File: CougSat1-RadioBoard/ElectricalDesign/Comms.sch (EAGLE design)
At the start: 416 parts, among them J1 230mm Antenna, J2 CougSat Card, J3 700mm Antenna, J4 SWD, Q1 CSD25402Q3A, Q12 DMN53D0LDW, Q2 CSD25402Q3A, Q3 DMN53D0LDW, Q9 DMN53D0LDW, U1 INA199C1, U10 HMC452QS16G, U11 AD8515, U12 AD7291, U13 AD8515, U14 LP5907MFX-3.1, U15 AD9761, U16 TXS0102DQM, U18 TXS0102DQM, U19 MMZ09332B, U2 LP5907MFX-3.1, U20 ADF4360, U21 HMC545A, U22 AD9761, U23 MAAM-011229, U24 AD8515, U25 MAAM-011229, U26 AD8345, U28 AD8348, U29 AD7291, U3 TPS61236, U30 TXS0102DQM, U31 MAAM-011229, U32 AD8515, U35 TXS0102DQM, U36 ADF4360, U37 MAAM-011229, U39 AD8515, U4 AD8346, U40 AD8515, U42 TXS0102DQM, U43 INA199C2, U44 TXS0102DQM, U45 TXS0102DQM, U46 TXS0102DQM, U47 TXS0102DQM, U48 AD7291, U49 AD8515, U5 ADF4360, U50 INA199C2, U51 LP5907MFX-3.1, U52 INA199C2, U53 INA199C1, U54 TXS0102DQM, U55 TXS0102DQM, U6 STM32L496VGT, U7 GRF2133, U8 IS25LP016D, U9 IS25LP016D, Y1 19.68MHz ±2.5ppm, Y2 8MHz ±10ppm, Y3 32.768kHz ±10ppm, Y4 19.68MHz ±2.5ppm, Y5 19.68MHz ±2.5ppm

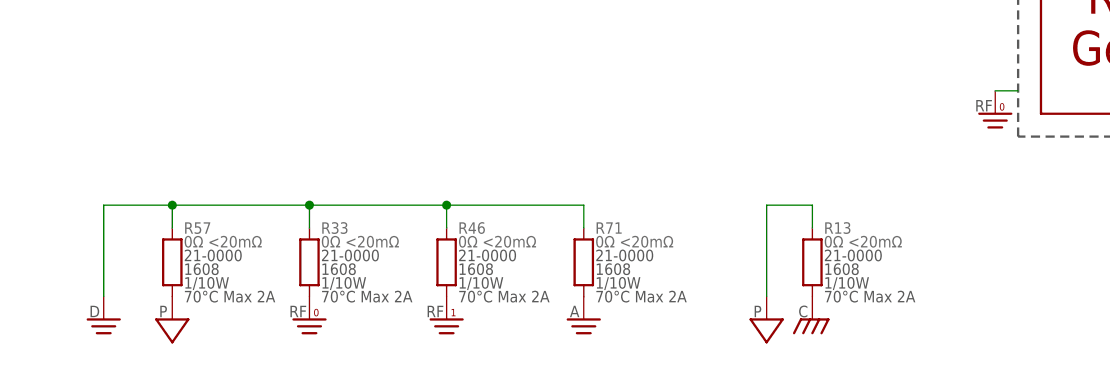
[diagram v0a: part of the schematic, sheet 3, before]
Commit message: Updated layout constraints and tests
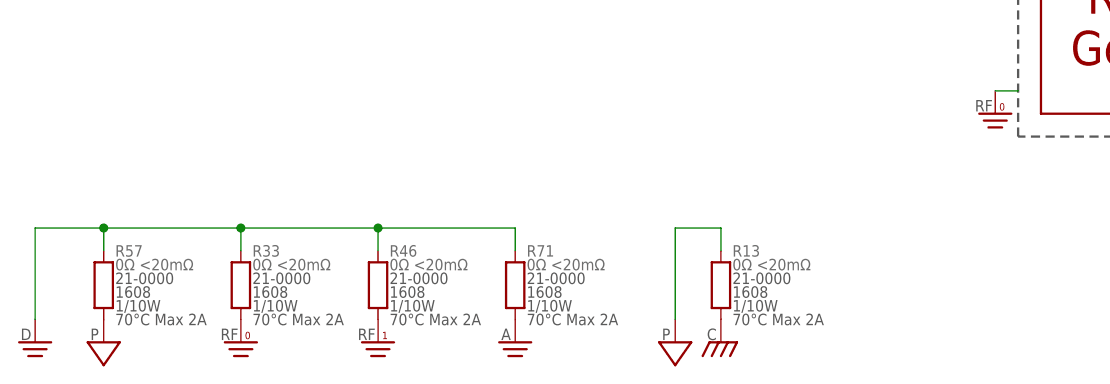
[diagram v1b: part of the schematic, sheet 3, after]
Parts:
- added RN4: 5kΩ 0.1%, CougsInSpace-Resistors:RES-H-PAIRED-5K-1616
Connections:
- net PA_PDET-700: now also RN4.B1
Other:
- moved on the sheet: C100, C93, FB6, R13, R33, R46, R57, R71, TP2

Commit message: Began part placement
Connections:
- removed net 3.3V_2: U20.AVDD, U20.CE, U20.DVDD, U20.VVCO
- net 3.1V_2: now also U20.AVDD, U20.CE, U20.DVDD, U20.VVCO
- net 3.3V_0: now also J2POWER.PR_3.3V-0; no longer J2POWER.PWR_CTRL_SW
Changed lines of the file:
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@@
 <class number="0" name="default" width="0" drill="0">
 </class>
-<class number="1" name="50Ohm" width="0.3" drill="0">
-<clearance class="1" value="0.16"/>
+<class number="1" name="50Ohm" width="0.22" drill="0">
+<clearance class="1" value="0.5"/>
 </class>
-<class number="2" name="200Ohm" width="0.16" drill="0">
-<clearance class="2" value="0.3"/>
+<class number="2" name="200Ohm" width="0.25" drill="0">
+<clearance class="2" value="0.6"/>
 </class>
 <class number="3" name="Supplies" width="0.25" drill="0">
@@
 <part name="DIA32" library="CougsInSpace-Aesthetics" deviceset="DIAGRAM-CONNECT_DOT" device=""/>
 <part name="DIA41" library="CougsInSpace-Aesthetics" deviceset="DIAGRAM-CONNECT_DOT" device=""/>
-<part name="SUPPLY129" library="CougsInSpace-PowerSymbols" deviceset="3.3V-2" device=""/>
 <part name="C5" library="CougsInSpace-Capacitors" deviceset="CAP-POL-V" device="-4028" technology="-47UF" value="47µF"/>
 <part name="J1" library="CougsInSpace-Connectors" deviceset="COAX" device="-U.FL" value="230mm Antenna"/>
@@
 <part name="R13" library="CougsInSpace-Resistors" deviceset="RES-V" device="-1608" technology="-0" value="0Ω &lt;20mΩ"/>
 <part name="RN4" library="CougsInSpace-Resistors" deviceset="RES-H-PAIRED" device="-1616" technology="-5K" value="5kΩ 0.1%"/>
+<part name="SUPPLY129" library="CougsInSpace-PowerSymbols" deviceset="3.1V-2" device=""/>
 </parts>
 <sheets>
@@
 </segment>
 <segment>
-<pinref part="J2" gate="POWER" pin="PWR_CTRL_SW"/>
 <pinref part="SUPPLY86" gate="G$1" pin="3.3V_0"/>
-<wire x1="241.3" y1="182.88" x2="246.38" y2="182.88" width="0.1524" layer="91"/>
 <wire x1="246.38" y1="182.88" x2="246.38" y2="185.42" width="0.1524" layer="91"/>
+<pinref part="J2" gate="POWER" pin="PR_3.3V-0"/>
+<wire x1="241.3" y1="180.34" x2="246.38" y2="180.34" width="0.1524" layer="91"/>
+<wire x1="246.38" y1="180.34" x2="246.38" y2="182.88" width="0.1524" layer="91"/>
 </segment>
 </net>
@@
 <attribute name="SKU" x="229.87" y="144.272" size="1.27" layer="97" align="center-left"/>
 </instance>
-<instance part="SUPPLY129" gate="G$1" x="127" y="175.26" smashed="yes">
-<attribute name="VALUE" x="127" y="178.816" size="1.27" layer="96" align="center"/>
-</instance>
 <instance part="Y4" gate="G$1" x="101.6" y="170.18" smashed="yes">
 <attribute name="NAME" x="101.6" y="176.53" size="1.778" layer="95" align="center"/>
@@
 <instance part="SUPPLY181" gate="G$1" x="15.24" y="45.72" smashed="yes"/>
 <instance part="SUPPLY182" gate="G$1" x="15.24" y="7.62" smashed="yes"/>
+<instance part="SUPPLY129" gate="G$1" x="127" y="175.26" smashed="yes">
+<attribute name="VALUE" x="127" y="178.816" size="1.27" layer="96" align="center"/>
+</instance>
 </instances>
 <busses>
@@
 </segment>
 </net>
-<net name="3.3V_2" class="0">
-<segment>
-<pinref part="U20" gate="G$1" pin="AVDD"/>
-<wire x1="129.54" y1="172.72" x2="127" y2="172.72" width="0.1524" layer="91"/>
-<pinref part="U20" gate="G$1" pin="DVDD"/>
-<wire x1="129.54" y1="170.18" x2="127" y2="170.18" width="0.1524" layer="91"/>
-<wire x1="127" y1="170.18" x2="127" y2="172.72" width="0.1524" layer="91"/>
-<pinref part="U20" gate="G$1" pin="VVCO"/>
-<wire x1="129.54" y1="167.64" x2="127" y2="167.64" width="0.1524" layer="91"/>
-<wire x1="127" y1="167.64" x2="127" y2="170.18" width="0.1524" layer="91"/>
-<junction x="127" y="170.18"/>
-<wire x1="127" y1="172.72" x2="127" y2="175.26" width="0.1524" layer="91"/>
-<junction x="127" y="172.72"/>
-<pinref part="U20" gate="G$1" pin="CE"/>
-<wire x1="129.54" y1="149.86" x2="127" y2="149.86" width="0.1524" layer="91"/>
-<wire x1="127" y1="149.86" x2="127" y2="167.64" width="0.1524" layer="91"/>
-<junction x="127" y="167.64"/>
-<pinref part="SUPPLY129" gate="G$1" pin="3.3V_2"/>
-</segment>
-</net>
 <net name="RFCLK_REFIN-DEMOD" class="0">
 <segment>
@@
 <pinref part="SUPPLY441" gate="G$1" pin="3.1V_2"/>
 </segment>
+<segment>
+<pinref part="U20" gate="G$1" pin="AVDD"/>
+<wire x1="129.54" y1="172.72" x2="127" y2="172.72" width="0.1524" layer="91"/>
+<pinref part="U20" gate="G$1" pin="DVDD"/>
+<wire x1="129.54" y1="170.18" x2="127" y2="170.18" width="0.1524" layer="91"/>
+<wire x1="127" y1="170.18" x2="127" y2="172.72" width="0.1524" layer="91"/>
+<pinref part="U20" gate="G$1" pin="VVCO"/>
+<wire x1="129.54" y1="167.64" x2="127" y2="167.64" width="0.1524" layer="91"/>
+<wire x1="127" y1="167.64" x2="127" y2="170.18" width="0.1524" layer="91"/>
+<junction x="127" y="170.18"/>
+<wire x1="127" y1="172.72" x2="127" y2="175.26" width="0.1524" layer="91"/>
+<junction x="127" y="172.72"/>
+<pinref part="U20" gate="G$1" pin="CE"/>
+<wire x1="129.54" y1="149.86" x2="127" y2="149.86" width="0.1524" layer="91"/>
+<wire x1="127" y1="149.86" x2="127" y2="167.64" width="0.1524" layer="91"/>
+<junction x="127" y="167.64"/>
+<pinref part="SUPPLY129" gate="G$1" pin="3.1V_2"/>
+</segment>
 </net>

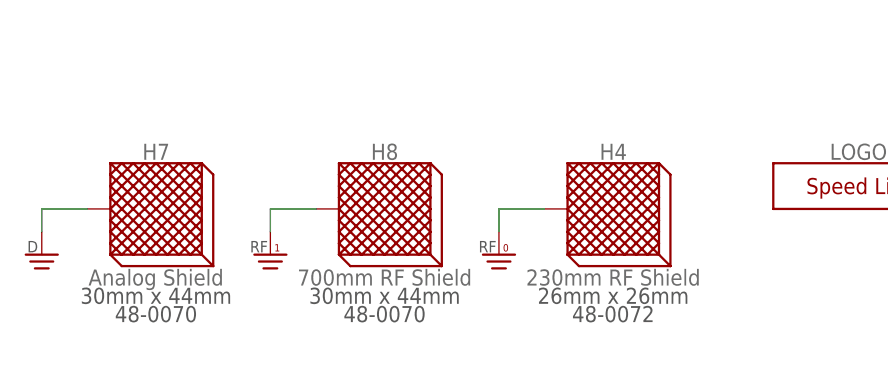
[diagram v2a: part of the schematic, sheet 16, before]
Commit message: Placed Comms parts
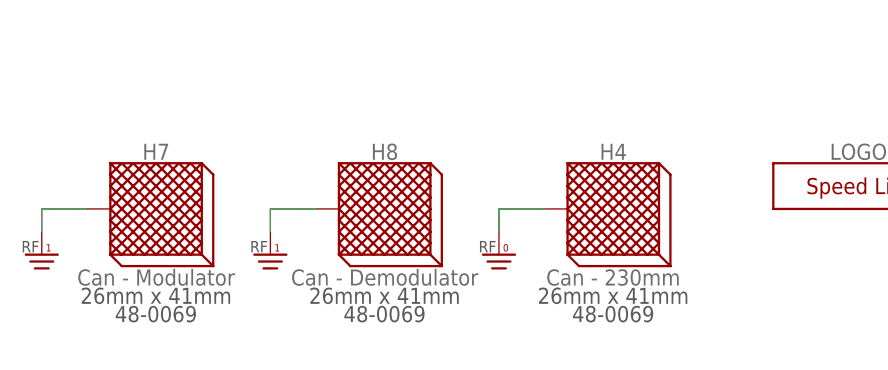
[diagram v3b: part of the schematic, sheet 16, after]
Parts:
- H4: value 230mm RF Shield -> Can - 230mm; device CougsInSpace-Hardware:SHIELDING-2626 -> CougsInSpace-Hardware:SHIELDING-2641
- H7: value Analog Shield -> Can - Modulator; device CougsInSpace-Hardware:SHIELDING-3044 -> CougsInSpace-Hardware:SHIELDING-2641
- H8: value 700mm RF Shield -> Can - Demodulator; device CougsInSpace-Hardware:SHIELDING-3044 -> CougsInSpace-Hardware:SHIELDING-2641
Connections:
- net DGND: no longer H7.SHIELD
- net RFGND-1: now also H7.SHIELD

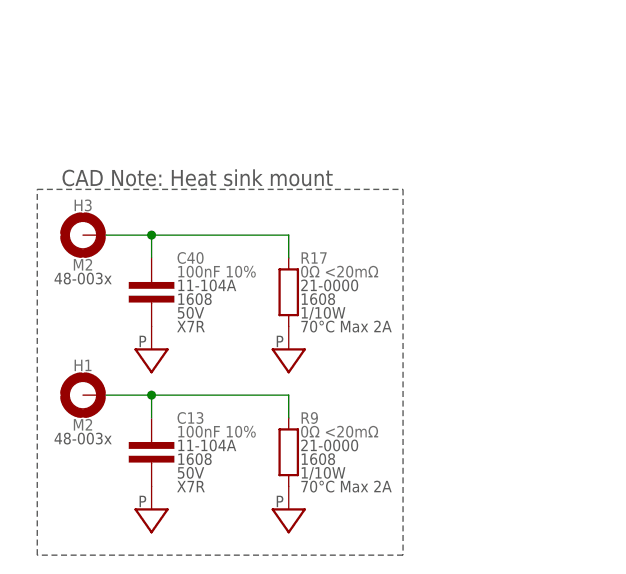
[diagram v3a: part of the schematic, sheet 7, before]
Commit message: Laid out RF traces
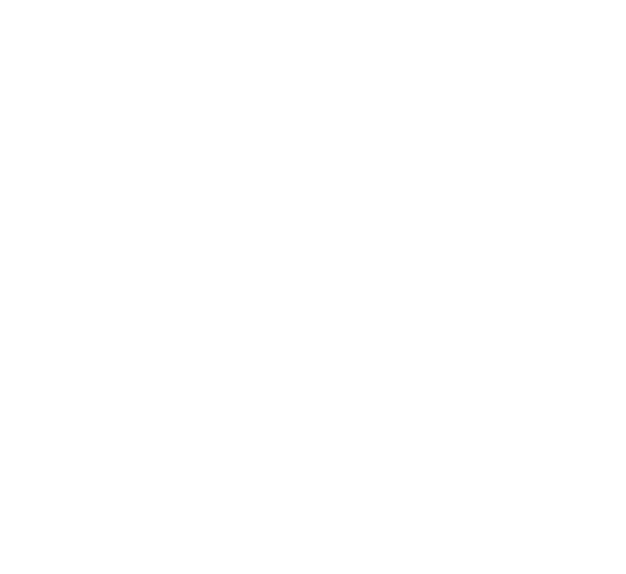
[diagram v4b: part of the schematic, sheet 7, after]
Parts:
- removed C13, C40: 100nF 10%, CougsInSpace-Capacitors:CAP-V-100NF-1608
- removed H1, H3: M2, CougsInSpace-Hardware:MOUNTING_HOLE-2.2
- removed R17, R9: 0Ω <20mΩ, CougsInSpace-Resistors:RES-V-0-1608
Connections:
- removed net CHASSIS_REG-0: C40.1, H3.MOUNT, R17.2
- removed net CHASSIS_REG-1: C13.1, H1.MOUNT, R9.2
- net PGND: no longer C13.2, C40.2, R17.1, R9.1

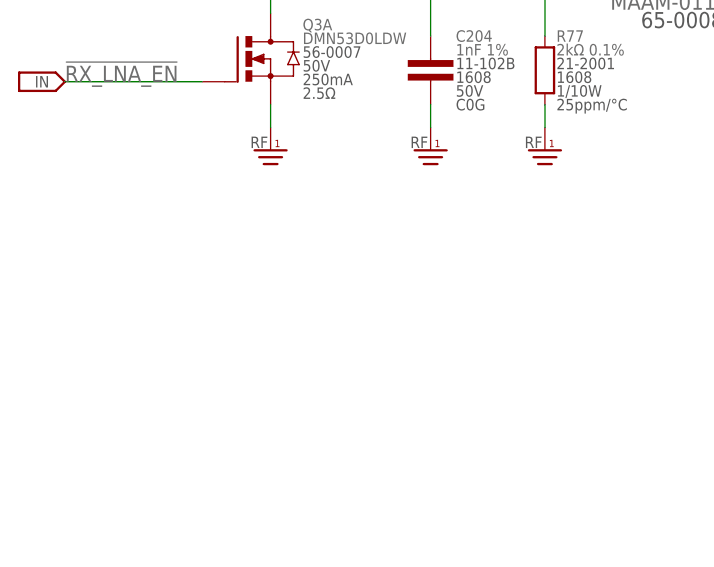
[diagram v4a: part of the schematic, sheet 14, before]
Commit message: Laid out decapaps for the RF chips
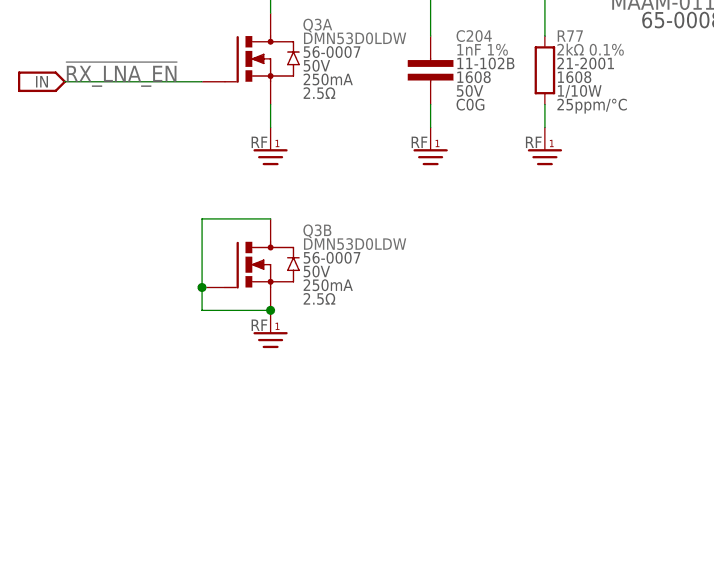
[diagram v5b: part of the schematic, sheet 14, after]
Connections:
- net RFGND-1: now also Q3B.D, Q3B.G, Q3B.S
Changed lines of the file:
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@@
 </variantdefs>
 <classes>
-<class number="0" name="default" width="0" drill="0">
+<class number="0" name="default" width="0.16" drill="0">
 </class>
 <class number="1" name="50Ohm" width="0.2" drill="0">
@@
 <part name="SUPPLY238" library="CougsInSpace-PowerSymbols" deviceset="3.1V-1" device=""/>
 <part name="SUPPLY239" library="CougsInSpace-PowerSymbols" deviceset="3.1V-1" device=""/>
-<part name="OFFSHEET92" library="CougsInSpace-Aesthetics" deviceset="OFF_SHEET-IN" device=""/>
-<part name="OFFSHEET94" library="CougsInSpace-Aesthetics" deviceset="OFF_SHEET-IN" device=""/>
 <part name="C151" library="CougsInSpace-Capacitors" deviceset="CAP-V" device="-1608" technology="-10PF" value="10pF 5%"/>
 <part name="C156" library="CougsInSpace-Capacitors" deviceset="CAP-V" device="-1608" technology="-18PF" value="18pF 1%"/>
@@
 <part name="SUPPLY129" library="CougsInSpace-PowerSymbols" deviceset="3.1V-2" device=""/>
 <part name="SUPPLY195" library="CougsInSpace-PowerSymbols" deviceset="RFGND-1" device=""/>
+<part name="SUPPLY197" library="CougsInSpace-PowerSymbols" deviceset="RFGND-1" device=""/>
+<part name="OFFSHEET92" library="CougsInSpace-Aesthetics" deviceset="OFF_SHEET-OUT" device=""/>
+<part name="OFFSHEET94" library="CougsInSpace-Aesthetics" deviceset="OFF_SHEET-OUT" device=""/>
 </parts>
 <sheets>
@@
 </instance>
 <instance part="OFFSHEET208" gate="G$1" x="251.46" y="142.24" smashed="yes" rot="MR0"/>
-<instance part="OFFSHEET92" gate="G$1" x="302.26" y="165.1" smashed="yes" rot="MR0"/>
-<instance part="OFFSHEET94" gate="G$1" x="302.26" y="167.64" smashed="yes" rot="MR0"/>
 <instance part="OFFSHEET115" gate="G$1" x="302.26" y="86.36" smashed="yes" rot="MR0"/>
 <instance part="OFFSHEET129" gate="G$1" x="48.26" y="86.36" smashed="yes" rot="MR0"/>
@@
 <attribute name="VALUE" x="228.6" y="140.716" size="1.27" layer="96" align="center"/>
 </instance>
+<instance part="OFFSHEET92" gate="G$1" x="302.26" y="167.64" smashed="yes" rot="MR0"/>
+<instance part="OFFSHEET94" gate="G$1" x="302.26" y="165.1" smashed="yes" rot="MR0"/>
 </instances>
 <busses>
@@
 </segment>
 </net>
-<net name="3.3V_6" class="0">
+<net name="3.3V_6" class="3">
 <segment>
 <wire x1="99.06" y1="172.72" x2="93.98" y2="172.72" width="0.1524" layer="91"/>
@@
 </segment>
 </net>
-<net name="3.3V_6" class="0">
+<net name="3.3V_6" class="3">
 <segment>
 <wire x1="121.92" y1="48.26" x2="121.92" y2="45.72" width="0.1524" layer="91"/>
@@
 </segment>
 </net>
-<net name="3.3V_5" class="0">
+<net name="3.3V_5" class="3">
 <segment>
 <wire x1="93.98" y1="45.72" x2="91.44" y2="45.72" width="0.1524" layer="91"/>
@@
 </segment>
 </net>
-<net name="3.3V_0" class="0">
+<net name="3.3V_0" class="3">
 <segment>
 <wire x1="93.98" y1="147.32" x2="91.44" y2="147.32" width="0.1524" layer="91"/>
@@
 </segment>
 </net>
-<net name="3.3V_6" class="0">
+<net name="3.3V_6" class="3">
 <segment>
 <pinref part="U48" gate="G$1" pin="VDRIVE"/>
@@
 </segment>
 </net>
-<net name="5.0V" class="0">
+<net name="5.0V" class="3">
 <segment>
 <wire x1="180.34" y1="137.16" x2="195.58" y2="137.16" width="0.1524" layer="91"/>
@@
 </segment>
 </net>
-<net name="5.0V" class="0">
+<net name="5.0V" class="3">
 <segment>
 <pinref part="SUPPLY270" gate="G$1" pin="5.0V"/>
@@
 </segment>
 </net>
-<net name="5.0V_1" class="0">
+<net name="5.0V_1" class="3">
 <segment>
 <pinref part="R119" gate="G$1" pin="1"/>
@@
 </segment>
 </net>
-<net name="3.1V_0" class="0">
+<net name="3.1V_0" class="3">
 <segment>
 <pinref part="U2" gate="G$1" pin="OUT"/>
@@
 </segment>
 </net>
-<net name="3.1V_1" class="0">
+<net name="3.1V_1" class="3">
 <segment>
 <pinref part="U14" gate="G$1" pin="OUT"/>
@@
 </segment>
 </net>
-<net name="3.1V_2" class="0">
+<net name="3.1V_2" class="3">
 <segment>
 <pinref part="U51" gate="G$1" pin="OUT"/>
@@
 </segment>
 </net>
-<net name="5.0V_0" class="0">
+<net name="5.0V_0" class="3">
 <segment>
 <pinref part="R5" gate="G$1" pin="1"/>
@@
 </segment>
 </net>
-<net name="3.3V_6" class="0">
+<net name="3.3V_6" class="3">
 <segment>
 <wire x1="81.28" y1="58.42" x2="81.28" y2="55.88" width="0.1524" layer="91"/>
@@
 </segment>
 </net>
-<net name="RFCLK_REFIN-230" class="1">
+<net name="RFCLK_REFIN-230" class="0">
 <segment>
 <wire x1="124.46" y1="170.18" x2="124.46" y2="162.56" width="0.1524" layer="91"/>
@@
 </segment>
 </net>
-<net name="REF_CLK_VDD-0" class="0">
+<net name="REF_CLK_VDD-0" class="3">
 <segment>
 <pinref part="Y1" gate="G$1" pin="VDD"/>
@@
 </segment>
 </net>
-<net name="RFCLK_REFOUT-230" class="1">
+<net name="RFCLK_REFOUT-230" class="0">
 <segment>
 <pinref part="Y1" gate="G$1" pin="OUT"/>
@@
 </segment>
 </net>
-<net name="3.1V_0" class="0">
+<net name="3.1V_0" class="3">
 <segment>
 <pinref part="U5" gate="G$1" pin="AVDD"/>
@@
 </segment>
 </net>
-<net name="RFCLK_L2-230" class="3">
+<net name="RFCLK_L2-230" class="0">
 <segment>
 <pinref part="U5" gate="G$1" pin="L2"/>
@@
 </segment>
 </net>
-<net name="RFCLK_L1-230" class="3">
+<net name="RFCLK_L1-230" class="0">
 <segment>
 <pinref part="U5" gate="G$1" pin="L1"/>
@@
 </segment>
 </net>
-<net name="3.3V_6" class="0">
+<net name="3.3V_6" class="3">
 <segment>
 <pinref part="U44" gate="G$1" pin="VCCA"/>
@@
 </segment>
 </net>
-<net name="REF_CLK_VDD-1" class="0">
+<net name="REF_CLK_VDD-1" class="3">
 <segment>
 <pinref part="Y5" gate="G$1" pin="VDD"/>
@@
 </segment>
 </net>
-<net name="3.1V_1" class="0">
+<net name="3.1V_1" class="3">
 <segment>
 <pinref part="FB9" gate="G$1" pin="2"/>
@@
 </segment>
 </net>
-<net name="RFCLK_REFOUT-MOD" class="1">
+<net name="RFCLK_REFOUT-MOD" class="0">
 <segment>
 <pinref part="Y5" gate="G$1" pin="OUT"/>
@@
 </segment>
 </net>
-<net name="3.3V_6" class="0">
+<net name="3.3V_6" class="3">
 <segment>
 <pinref part="U18" gate="G$1" pin="VCCA"/>
@@
 </segment>
 </net>
-<net name="RFCLK_REFIN-DEMOD" class="1">
+<net name="RFCLK_REFIN-DEMOD" class="0">
 <segment>
 <wire x1="124.46" y1="170.18" x2="124.46" y2="162.56" width="0.1524" layer="91"/>
@@
 </segment>
 </net>
-<net name="REF_CLK_VDD-2" class="0">
+<net name="REF_CLK_VDD-2" class="3">
 <segment>
 <pinref part="Y4" gate="G$1" pin="VDD"/>
@@
 </segment>
 </net>
-<net name="RFCLK_REFOUT-DEMOD" class="1">
+<net name="RFCLK_REFOUT-DEMOD" class="0">
 <segment>
 <pinref part="Y4" gate="G$1" pin="OUT"/>
@@
 </segment>
 </net>
-<net name="3.1V_2" class="0">
+<net name="3.1V_2" class="3">
 <segment>
 <pinref part="FB4" gate="G$1" pin="2"/>
@@
 </segment>
 </net>
-<net name="3.3V_6" class="0">
+<net name="3.3V_6" class="3">
 <segment>
 <pinref part="U55" gate="G$1" pin="VCCA"/>
@@
 </segment>
 </net>
-<net name="5.0V_0" class="0">
+<net name="5.0V_0" class="3">
 <segment>
 <pinref part="R87" gate="G$1" pin="2"/>
@@
 </segment>
 </net>
-<net name="3.1V_0" class="0">
+<net name="3.1V_0" class="3">
 <segment>
 <pinref part="R14" gate="G$1" pin="2"/>
@@
 </segment>
 </net>
-<net name="5.0V" class="0">
+<net name="5.0V" class="3">
 <segment>
 <pinref part="R47" gate="G$1" pin="2"/>
@@
 </segment>
 </net>
-<net name="5.0V_1" class="0">
+<net name="5.0V_1" class="3">
 <segment>
 <pinref part="L8" gate="G$1" pin="2"/>
@@
 </segment>
 </net>
-<net name="3.1V_1" class="0">
+<net name="3.1V_1" class="3">
 <segment>
 <pinref part="R75" gate="G$1" pin="2"/>
@@
 <attribute name="VALUE" x="99.06" y="168.656" size="1.27" layer="96" align="center"/>
 </instance>
+<instance part="SUPPLY197" gate="G$1" x="38.1" y="93.98" smashed="yes"/>
+<instance part="Q3" gate="B" x="38.1" y="101.6" smashed="yes">
+<attribute name="NAME" x="41.656" y="105.41" size="1.27" layer="95" align="center-left"/>
+<attribute name="VALUE" x="41.656" y="103.886" size="1.27" layer="96" align="center-left"/>
+<attribute name="SKU" x="41.656" y="102.362" size="1.27" layer="97" align="center-left"/>
+<attribute name="VDS" x="41.656" y="100.838" size="1.27" layer="97" align="center-left"/>
+<attribute name="CURRENT" x="41.656" y="99.314" size="1.27" layer="97" align="center-left"/>
+<attribute name="RDS" x="41.656" y="97.79" size="1.27" layer="97" align="center-left"/>
+</instance>
 </instances>
 <busses>
@@
 <pinref part="SUPPLY351" gate="G$1" pin="RFGND-1"/>
 </segment>
+<segment>
+<pinref part="SUPPLY197" gate="G$1" pin="RFGND-1"/>
+<wire x1="38.1" y1="106.68" x2="30.48" y2="106.68" width="0.1524" layer="91"/>
+<wire x1="30.48" y1="106.68" x2="30.48" y2="99.06" width="0.1524" layer="91"/>
+<wire x1="30.48" y1="99.06" x2="30.48" y2="96.52" width="0.1524" layer="91"/>
+<wire x1="30.48" y1="96.52" x2="38.1" y2="96.52" width="0.1524" layer="91"/>
+<pinref part="Q3" gate="B" pin="G"/>
+<junction x="30.48" y="99.06"/>
+<pinref part="Q3" gate="B" pin="D"/>
+<pinref part="Q3" gate="B" pin="S"/>
+<junction x="38.1" y="96.52"/>
+</segment>
 </net>
-<net name="3.1V_2" class="0">
+<net name="3.1V_2" class="3">
 <segment>
 <pinref part="R67" gate="G$1" pin="2"/>
@@
 </segment>
 </net>
-<net name="DEMOD_700_BALUN_PRIMARY1" class="1">
+<net name="DEMOD_700_BALUN_PRIMARY1" class="2">
 <segment>
 <pinref part="C124" gate="G$1" pin="2"/>
@@
 </segment>
 </net>
-<net name="3.1V_2" class="0">
+<net name="3.1V_2" class="3">
 <segment>
 <pinref part="R59" gate="G$1" pin="2"/>
